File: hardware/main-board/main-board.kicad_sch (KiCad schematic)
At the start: 91 parts, among them J1 USB_C_Receptacle_USB2.0, J2 DNI, J3 Display Connector, J4 Conn_01x04, SW1 SW_Push, SW2 SW_Push, SW3 SW_Push, SW4 SW_Push, SW5 SW_Detect, SW6 SW_Boot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

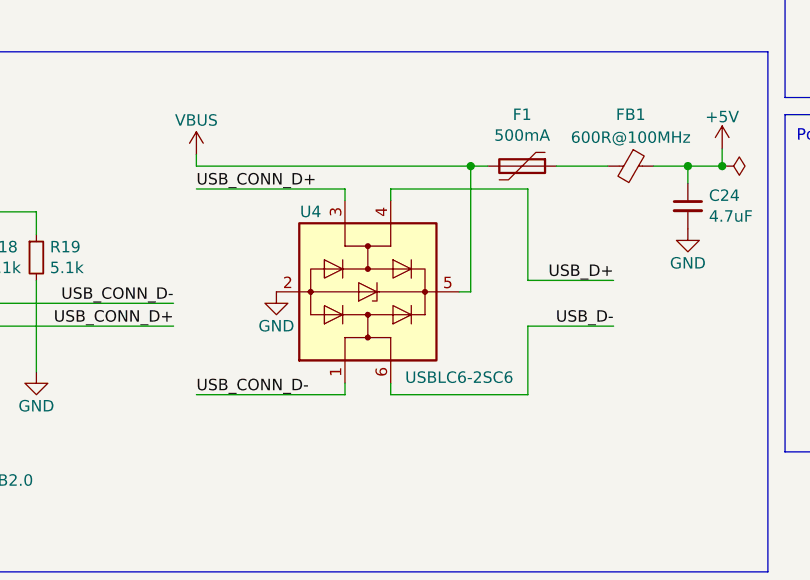
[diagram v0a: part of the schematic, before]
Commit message: Update symbols changed in library
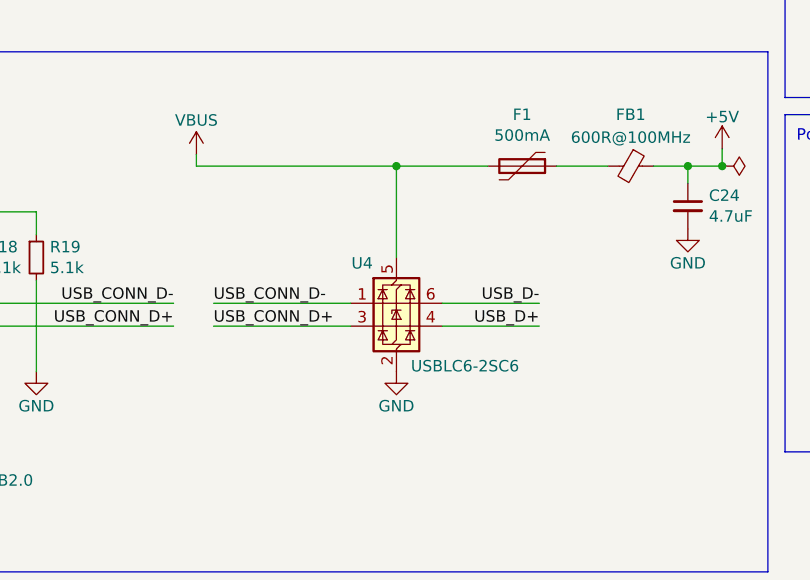
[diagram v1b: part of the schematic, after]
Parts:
- J1: symbol Connector:USB_C_Receptacle_USB2.0 -> Connector:USB_C_Receptacle_USB2.0_16P
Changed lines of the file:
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@@
 	)
 	(junction
+		(at 93.98 156.21)
+		(diameter 0)
+		(color 0 0 0 0)
+	)
+	(junction
 		(at 179.07 82.55)
 		(diameter 0)
@@
 		(color 0 0 0 0)
 	)
-	(junction
-		(at 102.235 156.21)
-		(diameter 0)
-		(color 0 0 0 0)
-	)
 	(no_connect
 		(at 170.18 121.285)
@@
 	(wire
 		(pts
+			(xy 93.98 156.21) (xy 104.14 156.21)
+		)
+		(stroke
+			(width 0)
+			(type default)
+		)
+	)
+	(wire
+		(pts
 			(xy 313.69 143.51) (xy 315.595 143.51)
 		)
@@
 	(wire
 		(pts
-			(xy 102.235 156.21) (xy 104.14 156.21)
-		)
-		(stroke
-			(width 0)
-			(type default)
-		)
-	)
-	(wire
-		(pts
-			(xy 108.585 181.61) (xy 108.585 173.99)
+			(xy 71.755 156.21) (xy 93.98 156.21)
 		)
 		(stroke
@@
 	(wire
 		(pts
-			(xy 108.585 158.75) (xy 108.585 168.91)
-		)
-		(stroke
-			(width 0)
-			(type default)
-		)
-	)
-	(wire
-		(pts
-			(xy 108.585 168.91) (xy 118.11 168.91)
-		)
-		(stroke
-			(width 0)
-			(type default)
-		)
-	)
-	(wire
-		(pts
 			(xy 186.055 123.825) (xy 187.96 123.825)
 		)
@@
 	(wire
 		(pts
-			(xy 93.345 181.61) (xy 108.585 181.61)
-		)
-		(stroke
-			(width 0)
-			(type default)
-		)
-	)
-	(wire
-		(pts
 			(xy 263.525 35.56) (xy 263.525 36.195)
 		)
@@
 	(wire
 		(pts
-			(xy 93.345 158.75) (xy 108.585 158.75)
-		)
-		(stroke
-			(width 0)
-			(type default)
-		)
-	)
-	(wire
-		(pts
 			(xy 37.465 83.185) (xy 39.37 83.185)
 		)
@@
 	(wire
 		(pts
-			(xy 71.755 158.75) (xy 88.265 158.75)
-		)
-		(stroke
-			(width 0)
-			(type default)
-		)
-	)
-	(wire
-		(pts
 			(xy 279.4 140.335) (xy 279.4 143.51)
 		)
@@
 	(wire
 		(pts
-			(xy 102.235 170.18) (xy 100.965 170.18)
-		)
-		(stroke
-			(width 0)
-			(type default)
-		)
-	)
-	(wire
-		(pts
 			(xy 199.39 120.015) (xy 199.39 121.285)
 		)
@@
 	(wire
 		(pts
-			(xy 108.585 173.99) (xy 118.11 173.99)
+			(xy 53.975 161.29) (xy 53.975 163.83)
 		)
 		(stroke
@@
 	(wire
 		(pts
-			(xy 53.975 161.29) (xy 53.975 163.83)
+			(xy 37.465 111.76) (xy 40.005 111.76)
 		)
 		(stroke
@@
 	(wire
 		(pts
-			(xy 37.465 111.76) (xy 40.005 111.76)
+			(xy 322.58 27.94) (xy 322.58 30.48)
 		)
 		(stroke
@@
 	(wire
 		(pts
-			(xy 322.58 27.94) (xy 322.58 30.48)
+			(xy 201.93 165.735) (xy 204.47 165.735)
 		)
 		(stroke
@@
 	(wire
 		(pts
-			(xy 201.93 165.735) (xy 204.47 165.735)
+			(xy 93.98 156.21) (xy 93.98 166.37)
 		)
 		(stroke
@@
 	(wire
 		(pts
+			(xy 73.66 171.45) (xy 88.9 171.45)
+		)
+		(stroke
+			(width 0)
+			(type default)
+		)
+	)
+	(wire
+		(pts
 			(xy 163.83 34.925) (xy 153.67 34.925)
 		)
@@
 	(wire
 		(pts
-			(xy 71.755 156.21) (xy 102.235 156.21)
-		)
-		(stroke
-			(width 0)
-			(type default)
-		)
-	)
-	(wire
-		(pts
 			(xy 170.18 111.125) (xy 206.375 111.125)
 		)
@@
 	(wire
 		(pts
-			(xy 71.755 181.61) (xy 88.265 181.61)
-		)
-		(stroke
-			(width 0)
-			(type default)
-		)
-	)
-	(wire
-		(pts
 			(xy 116.84 42.545) (xy 109.22 42.545)
 		)
@@
 	(wire
 		(pts
-			(xy 322.58 45.72) (xy 329.565 45.72)
+			(xy 73.66 173.99) (xy 88.9 173.99)
 		)
 		(stroke
@@
 	(wire
 		(pts
-			(xy 294.005 55.88) (xy 302.26 55.88)
+			(xy 322.58 45.72) (xy 329.565 45.72)
 		)
 		(stroke
@@
 	(wire
 		(pts
-			(xy 102.235 156.21) (xy 102.235 170.18)
+			(xy 294.005 55.88) (xy 302.26 55.88)
 		)
 		(stroke
@@
 	(wire
 		(pts
-			(xy 93.345 180.34) (xy 93.345 181.61)
-		)
-		(stroke
-			(width 0)
-			(type default)
-		)
-	)
-	(wire
-		(pts
 			(xy 168.91 87.63) (xy 168.91 88.9)
 		)
@@
 	(wire
 		(pts
+			(xy 99.06 171.45) (xy 109.855 171.45)
+		)
+		(stroke
+			(width 0)
+			(type default)
+		)
+	)
+	(wire
+		(pts
 			(xy 294.005 120.015) (xy 294.005 122.555)
 		)
@@
 	(wire
 		(pts
-			(xy 93.345 160.02) (xy 93.345 158.75)
-		)
-		(stroke
-			(width 0)
-			(type default)
-		)
-	)
-	(wire
-		(pts
 			(xy 17.145 91.44) (xy 27.305 91.44)
 		)
@@
 	(wire
 		(pts
-			(xy 88.265 158.75) (xy 88.265 160.02)
-		)
-		(stroke
-			(width 0)
-			(type default)
-		)
-	)
-	(wire
-		(pts
 			(xy 203.2 42.545) (xy 191.77 42.545)
 		)
@@
 	(wire
 		(pts
-			(xy 88.265 181.61) (xy 88.265 180.34)
+			(xy 99.06 173.99) (xy 109.855 173.99)
 		)
 		(stroke
@@
 	)
 	(label "USB_D-"
-		(at 118.11 173.99 180)
+		(at 109.855 171.45 180)
 		(fields_autoplaced yes)
 		(effects
@@
 	)
 	(label "USB_CONN_D+"
-		(at 71.755 158.75 0)
+		(at 73.66 173.99 0)
 		(fields_autoplaced yes)
 		(effects
@@
 	)
 	(label "USB_D+"
-		(at 118.11 168.91 180)
+		(at 109.855 173.99 180)
 		(fields_autoplaced yes)
 		(effects
@@
 	)
 	(label "USB_CONN_D-"
-		(at 71.755 181.61 0)
+		(at 73.66 171.45 0)
 		(fields_autoplaced yes)
 		(effects
@@
 	(symbol
 		(lib_id "Power_Protection:USBLC6-2SC6")
-		(at 90.805 170.18 270)
-		(mirror x)
+		(at 93.98 171.45 0)
 		(unit 1)
 		(exclude_from_sim no)
@@
 		(dnp no)
 		(property "Reference" "U4"
-			(at 84.455 161.29 90)
+			(at 90.17 167.005 0)
 			(effects
 				(font
@@
 		)
 		(property "Value" "USBLC6-2SC6"
-			(at 100.965 179.705 90)
+			(at 101.6 178.435 0)
 			(effects
 				(font
@@
 		)
 		(property "Footprint" "Package_TO_SOT_SMD:SOT-23-6"
-			(at 78.105 170.18 0)
+			(at 93.98 184.15 0)
 			(effects
 				(font
@@
 		)
 		(property "Datasheet" "https://www.st.com/resource/en/datasheet/usblc6-2.pdf"
-			(at 99.695 165.1 0)
+			(at 99.06 162.56 0)
 			(effects
 				(font
@@
 		)
 		(property "Description" "TVS DIODE 5.25V 17V SOT23-6"
-			(at 90.805 170.18 0)
+			(at 93.98 171.45 0)
 			(effects
 				(font
@@
 		)
 		(property "Manufacturer" "STMicroelectronics"
-			(at 90.805 170.18 0)
+			(at 93.98 171.45 0)
 			(effects
 				(font
@@
 		)
 		(property "Manufacturer PN" "USBLC6-2SC6"
-			(at 90.805 170.18 0)
+			(at 93.98 171.45 0)
 			(effects
 				(font
@@
 		)
 		(property "Supplier" "LCSC"
-			(at 90.805 170.18 0)
+			(at 93.98 171.45 0)
 			(effects
 				(font
@@
 		)
 		(property "Supplier PN" "C7519"
-			(at 90.805 170.18 0)
+			(at 93.98 171.45 0)
 			(effects
 				(font
@@
 	(symbol
 		(lib_id "power:GND")
-		(at 80.645 170.18 0)
+		(at 93.98 179.07 0)
 		(unit 1)
 		(exclude_from_sim no)
@@
 		(dnp no)
 		(property "Reference" "#PWR0111"
-			(at 80.645 176.53 0)
+			(at 93.98 185.42 0)
 			(effects
 				(font
@@
 		)
 		(property "Value" "GND"
-			(at 80.645 173.99 0)
+			(at 93.98 182.88 0)
 			(effects
 				(font
@@
 		)
 		(property "Footprint" ""
-			(at 80.645 170.18 0)
+			(at 93.98 179.07 0)
 			(effects
 				(font
@@
 		)
 		(property "Datasheet" ""
-			(at 80.645 170.18 0)
+			(at 93.98 179.07 0)
 			(effects
 				(font
@@
 		)
 		(property "Description" "Power symbol creates a global label with name \"GND\" , ground"
-			(at 80.645 170.18 0)
+			(at 93.98 179.07 0)
 			(effects
 				(font
@@
 	)
 	(symbol
-		(lib_id "Connector:USB_C_Receptacle_USB2.0")
+		(lib_id "Connector:USB_C_Receptacle_USB2.0_16P")
 		(at 28.575 171.45 0)
 		(unit 1)

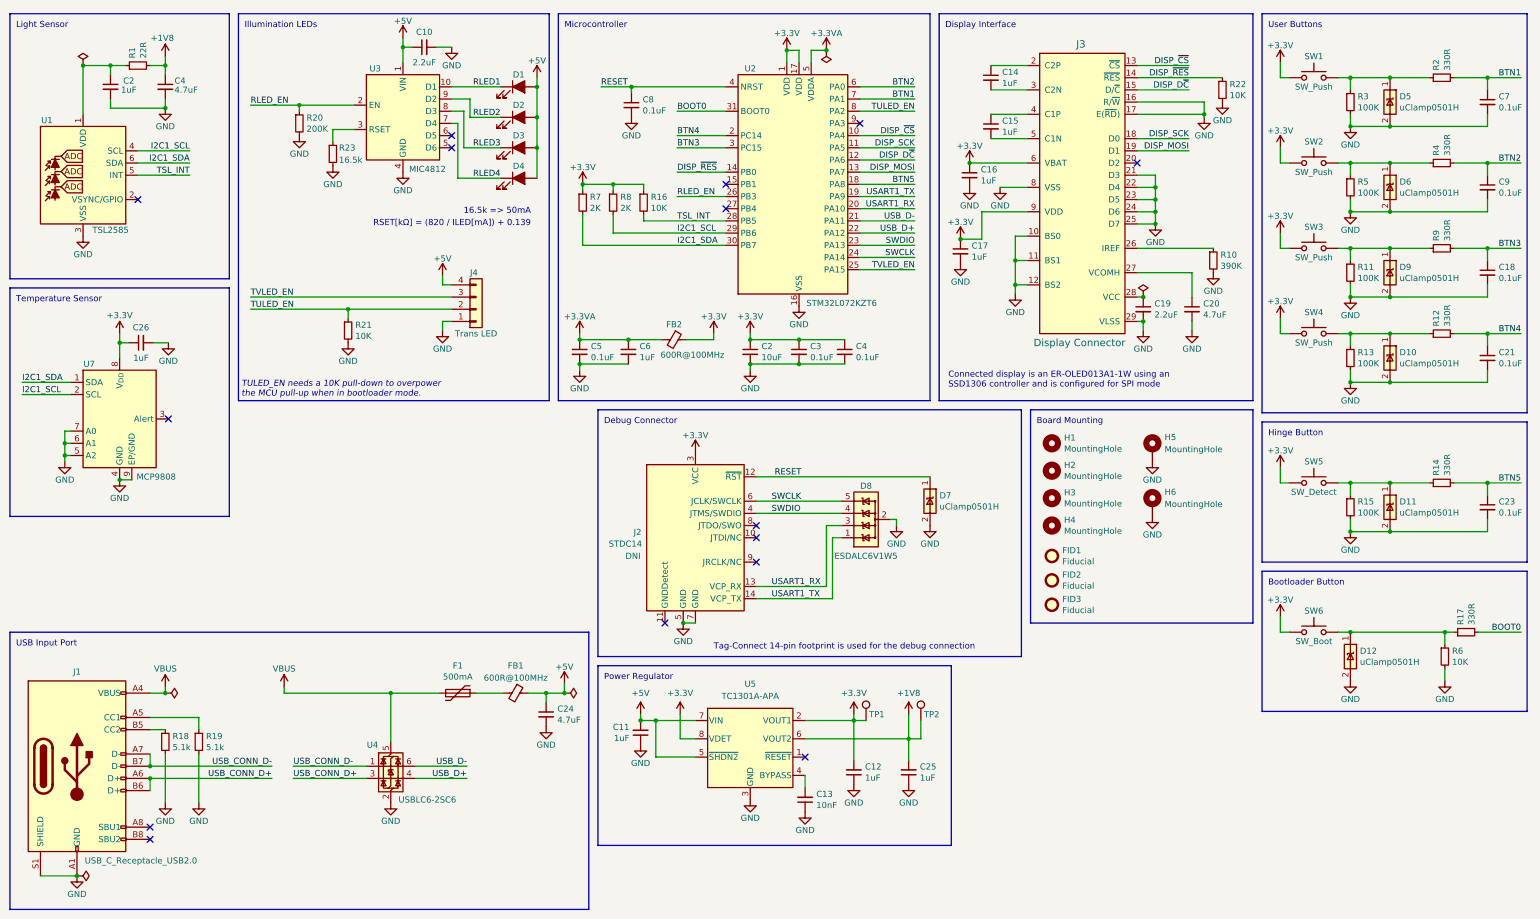
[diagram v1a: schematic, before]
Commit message: Update main board to match common conventions from current projects
Changed all single-line TVS diodes to the ESD321
Changed ferrite beads to the new common part.
Added a 10nF filter capacitor to VBus.
Made all 10nF filter capacitors now 0603 sized.
Changed all vias to new common sizes.
Changed zone clearance settings to new common values.
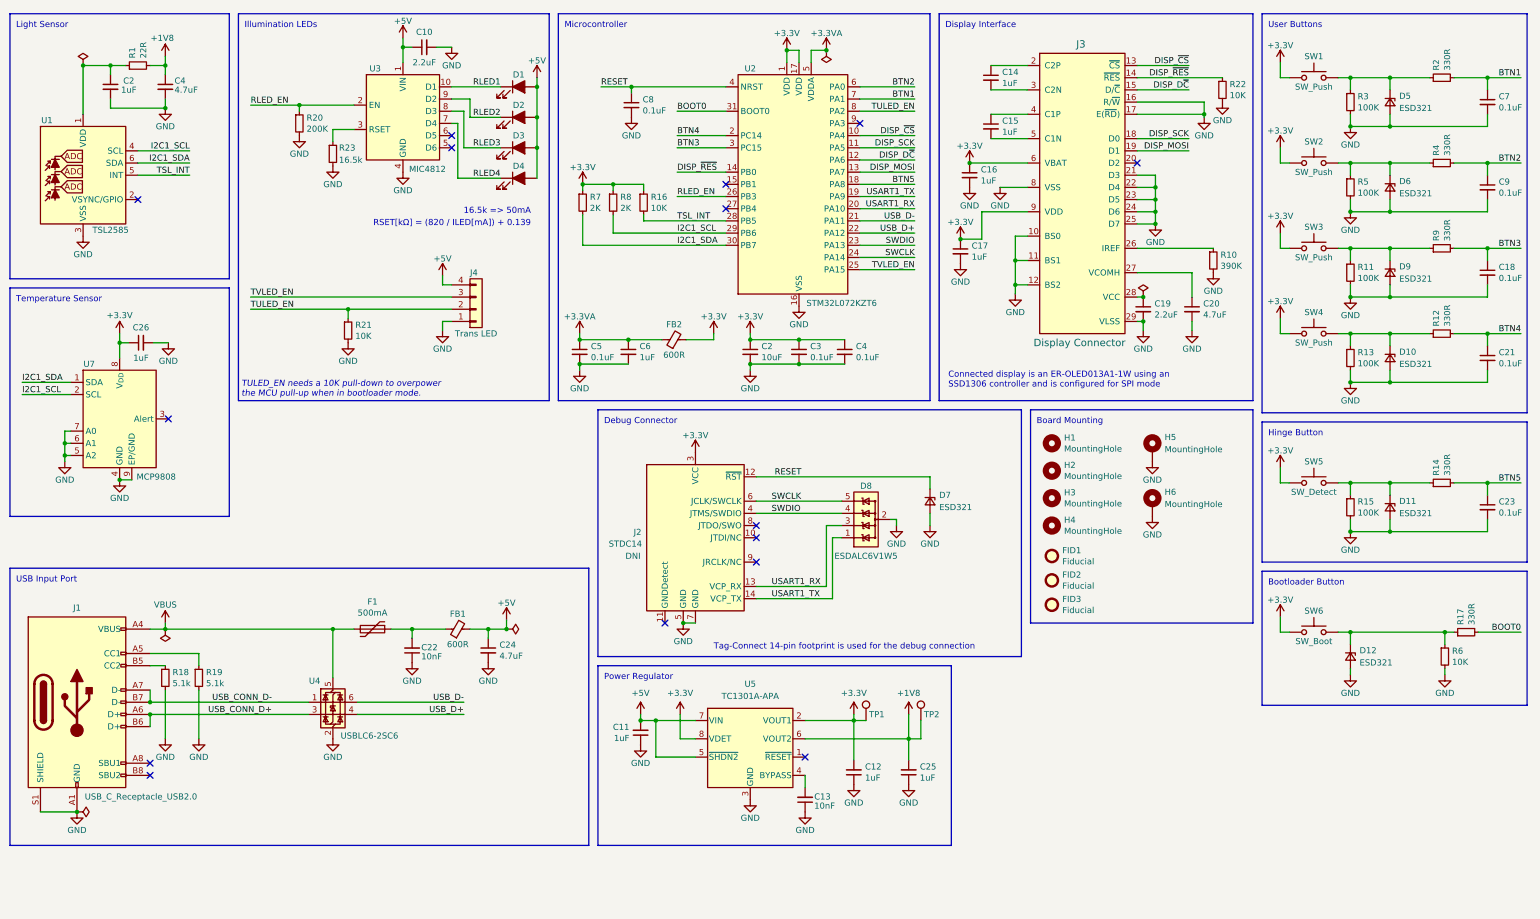
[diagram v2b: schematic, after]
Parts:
- removed D10, D11, D12, D5, D6, D7, D9: uClamp0501H, Diode_SMD:D_SOD-523, symbol Project:uClamp3301H
- added C22: 10nF, Capacitor_SMD:C_0603_1608Metric, symbol Device:C_Small
- added D10, D11, D12, D5, D6, D7, D9: ESD321, lib_fp:D_TI_SOD-523_DYA0002A, symbol Device:D_Zener_Small
- C13: footprint Capacitor_SMD:C_0805_2012Metric -> Capacitor_SMD:C_0603_1608Metric; Manufacturer Samsung Electro-Mechanic -> YAGEO; Manufacturer PN CL21B103KBANNNC -> CC0603KRX7R8BB103; Supplier PN 1276-1015-1-ND -> 311-1360-1-ND
- FB1, FB2: value 600R@100MHz -> 600R; Manufacturer TDK Corporation -> Würth Elektronik; Manufacturer PN MMZ1608R601ATD25 -> 742792651; Supplier PN 445-MMZ1608R601ATD25CT-ND -> 732-1593-1-ND
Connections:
- net +3.3V: now also FB2.2; no longer FB2.1
- net +3.3VA: now also FB2.1; no longer FB2.2
- net +5V: now also FB1.2; no longer FB1.1
- net GND: now also C22.1, D10.2 (A), D11.2 (A), D12.2 (A), D5.2 (A), D6.2 (A), D7.2 (A), D9.2 (A)
- net RESET: now also D7.1 (K)
- net at R2.1, R3.1, SW1.2: now also D5.1 (K)
- net at R4.1, R5.1, SW2.2: now also D6.1 (K)
- net at R17.1, R6.1, SW6.2: now also D12.1 (K)
- net at F1.1: now also FB1.1, C22.2; no longer FB1.2
- net at R11.1, R9.1, SW3.2: now also D9.1 (K)
- net at R12.1, R13.1, SW4.2: now also D10.1 (K)
- net at R14.1, R15.1, SW5.2: now also D11.1 (K)
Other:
- moved on the sheet: C24, F1, J1, R18, R19, U4

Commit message: Split schematic into multiple files
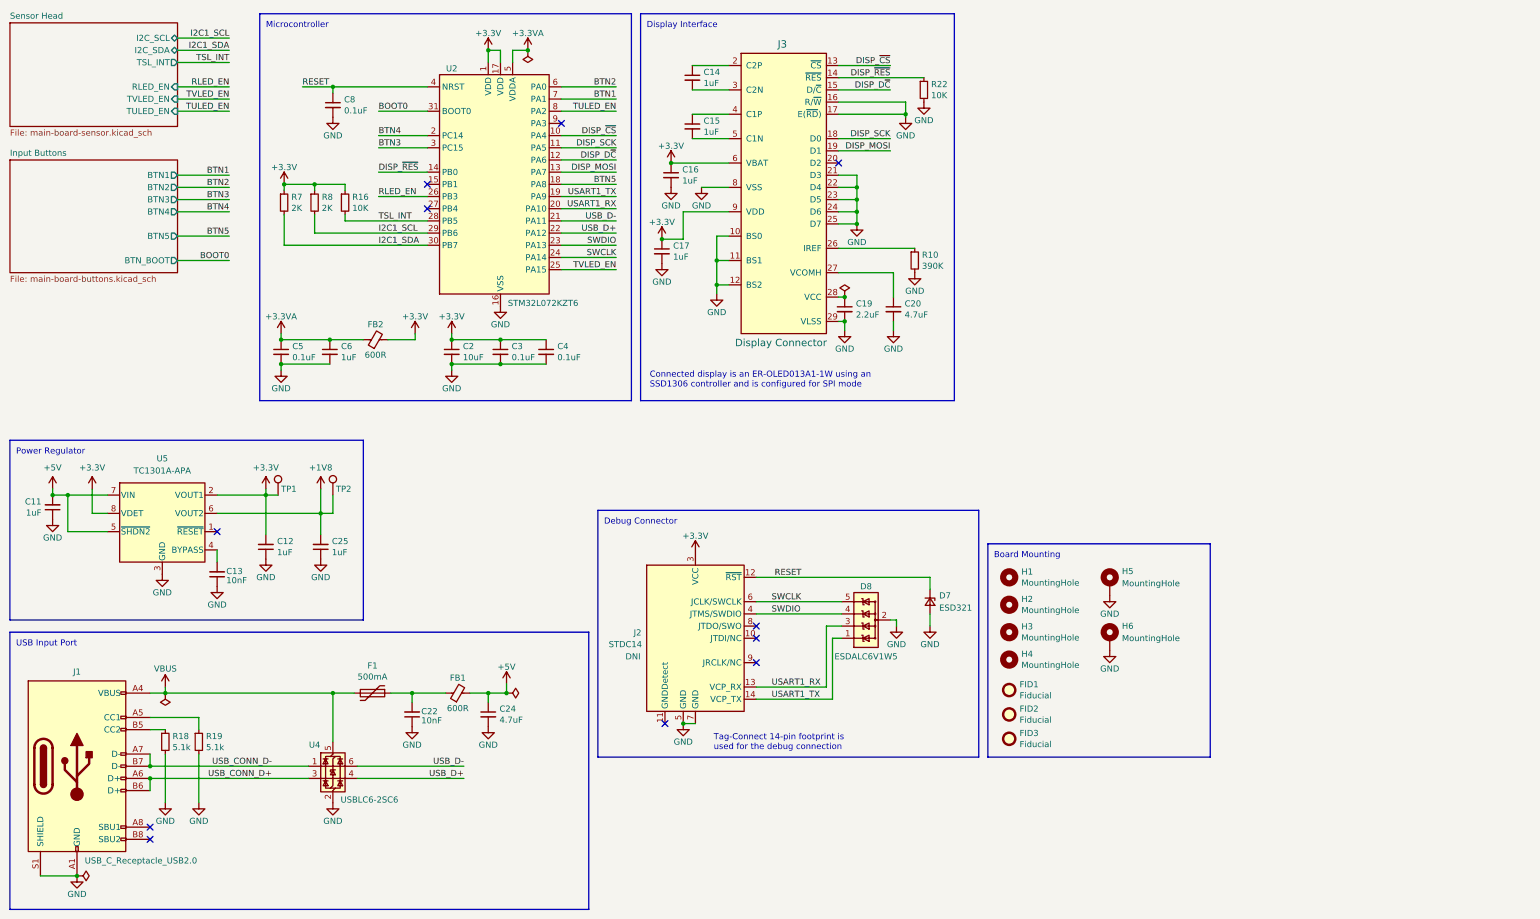
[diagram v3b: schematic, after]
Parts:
- removed C10: 2.2uF, Capacitor_SMD:C_0603_1608Metric, symbol Device:C_Small
- removed C18, C21, C23, C7, C9: 0.1uF, Capacitor_SMD:C_0603_1608Metric, symbol Device:C_Small
- removed C2, C26: 1uF, Capacitor_SMD:C_0402_1005Metric, symbol Device:C_Small
- removed C4: 4.7uF, Capacitor_SMD:C_0402_1005Metric, symbol Device:C_Small
- removed D1, D2, D3, D4: LED, lib_fp:SunLike_LED_S1S0, symbol Device:LED_Filled
- removed D10, D11, D12, D5, D6, D9: ESD321, lib_fp:D_TI_SOD-523_DYA0002A, symbol Device:D_Zener_Small
- removed J4: Conn_01x04, Connector_JST:JST_SH_BM04B-SRSS-TB_1x04-1MP_P1.00mm_Vertical, symbol Connector_Generic:Conn_01x04
- removed R1: 22R, Resistor_SMD:R_0402_1005Metric, symbol Device:R_Small
- removed R11, R13, R15, R3, R5: 100K, Resistor_SMD:R_0603_1608Metric, symbol Device:R_Small
- removed R12, R14, R17, R2, R4, R9: 330R, Resistor_SMD:R_0603_1608Metric, symbol Device:R_Small
- removed R20: 200K, Resistor_SMD:R_0603_1608Metric, symbol Device:R_Small
- removed R21, R6: 10K, Resistor_SMD:R_0603_1608Metric, symbol Device:R_Small
- removed R23: 16.5k, Resistor_SMD:R_0603_1608Metric, symbol Device:R_Small
- removed SW1, SW2, SW3, SW4: SW_Push, lib_fp:ESwitch_TL1105_6mm_H7.5mm, symbol Switch:SW_Push
- removed SW5: SW_Detect, lib_fp:CK_KSU213WLFG, symbol Switch:SW_Push
- removed SW6: SW_Boot, lib_fp:Panasonic_EVQP7C_EVQP7L, symbol Switch:SW_Push
- removed U1: TSL2585, lib_fp:AMS_TSL2585_OLGA-6_2x1mm_P0.65mm, symbol Project:TSL2585
- removed U3: MIC4812, lib_fp:Micrel_MSOP-10-1EP_3x3mm_P0.5mm_EP1.73x1.7mm_ThermalVias, symbol Project:MIC4812
- removed U7: MCP9808, Package_DFN_QFN:DFN-8-1EP_3x2mm_P0.5mm_EP1.7x1.4mm, symbol Sensor_Temperature:MCP9808_DFN
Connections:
- no-connect marks 15 -> 11
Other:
- added sheet Input Buttons (main-board-buttons.kicad_sch)
- added sheet Sensor Head (main-board-sensor.kicad_sch)
- note removed: "16.5k => 50mA"
- note removed: "Bootloader Button"
- note removed: "Hinge Button"
- note removed: "Illumination LEDs"
- note removed: "Light Sensor"
- note removed: "RSET[kΩ] = (820 / ILED[mA]) + 0.139"
- note removed: "TULED_EN needs a 10K pull-down to overpower the MCU pull-up when in bootloader mode."
- note removed: "Temperature Sensor"
- note removed: "User Buttons"
- moved on the sheet: C11, C12, C13, C14, C15, C16, C17, C19, C2, C20, C22, C24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
